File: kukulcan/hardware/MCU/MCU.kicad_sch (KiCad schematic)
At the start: 88 parts, among them J1 Barrel_Jack_5V_In, J2 Barrel_Jack_5V_In, J3 USB_C_Receptacle, J4 SMA_GNSS, Q1 AO3401A, U1 TLV1117-33, U2 W25Q256JVEIQ, U3 ESP32-S3R8, U4 BNO055, U5 NEO-M8N, U6 BMI088, U7 BME280, X1 40MHz, Y1 32.768kHz

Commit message: fix(kukulcan): led resistors fix
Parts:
- R3: value 1k/5% -> 100R/5%
- R4: value 1k/5% -> 220R/5%
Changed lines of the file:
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@@
 			)
 		)
-		(property "Value" "1k/5%"
+		(property "Value" "100R/5%"
 			(at 94.996 107.442 90)
 			(effects
@@
 			)
 		)
-		(property "Value" "1k/5%"
+		(property "Value" "220R/5%"
 			(at 134.366 107.442 90)
 			(effects

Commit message: fix(kukulcan): led resistors fix2
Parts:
- R3: value 100R/5% -> 1k/5%
- R4: value 220R/5% -> 1k/5%
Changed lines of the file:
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@@
 			)
 		)
-		(property "Value" "100R/5%"
+		(property "Value" "1k/5%"
 			(at 94.996 107.442 90)
 			(effects
@@
 			)
 		)
-		(property "Value" "220R/5%"
+		(property "Value" "1k/5%"
 			(at 134.366 107.442 90)
 			(effects

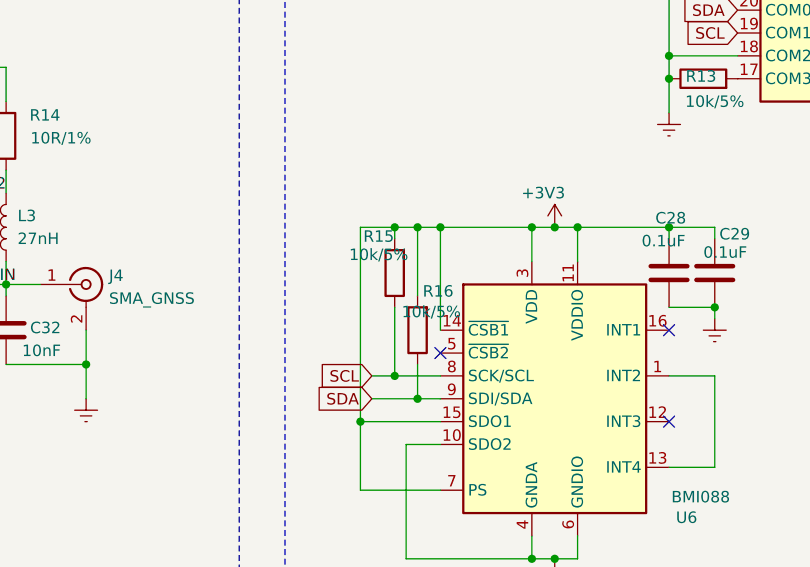
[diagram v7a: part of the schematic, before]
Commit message: fix(kukulcan): i2c pull-up
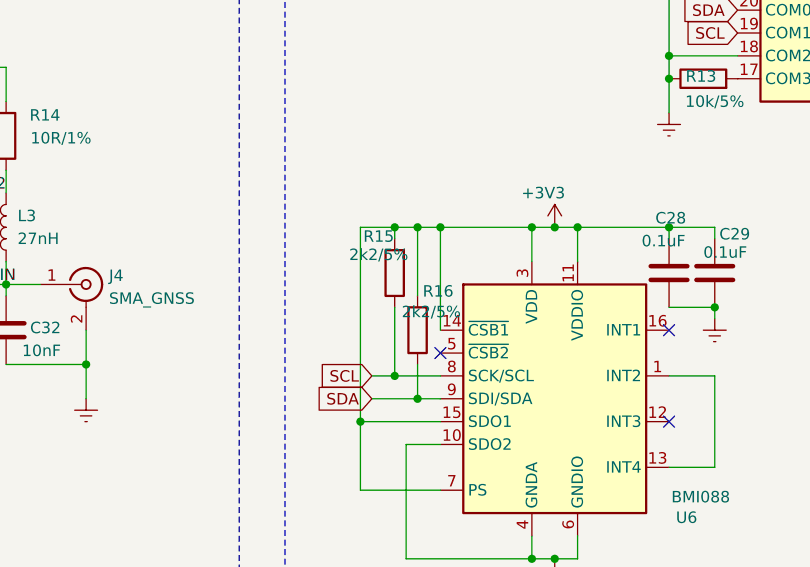
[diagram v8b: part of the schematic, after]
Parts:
- R15, R16: value 10k/5% -> 2k2/5%
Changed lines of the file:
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@@
 			)
 		)
-		(property "Value" "10k/5%"
+		(property "Value" "2k2/5%"
 			(at 127.254 222.758 0)
 			(effects
@@
 			)
 		)
-		(property "Value" "10k/5%"
+		(property "Value" "2k2/5%"
 			(at 121.412 216.408 0)
 			(effects
